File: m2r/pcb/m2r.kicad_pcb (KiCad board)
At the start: 2 copper layers, 87 parts, among them IC1 ADP3338, IC2 ADP3335, IC3 ADuM1201, IC4 ADuM1201, P1 CONN_2, P2 CONN_2, P7 CONN_2, X9 8M

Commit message: a good looking ratsnest
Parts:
- removed X9: 8M, Crystals:Crystal_HC49-U_Vertical
- added ANT1: JDGA_QUAD_V, m2r:JDGA_QUAD_V, F.Cu at (125.0, 61.5)
- added C35: 15p, m2r:C0603, F.Cu at (132.2, 110.2)
- added C36: 15p, m2r:C0603, F.Cu at (127.5, 110.2)
- added IC10: STM32F303C, m2r:LQFP48, F.Cu at (127.8, 102.0)
- added IC11: ADP3333, m2r:MSOP8, F.Cu at (119.8, 85.5)
- added IC5: ADuM1201, m2r:SOIC8, F.Cu at (137.2, 79.2)
- added IC6: MTX2, m2r:MTX2, F.Cu at (164.5, 98.0)
- added IC7: ADL5324, m2r:SOT89-3, F.Cu at (156.0, 81.5)
- added IC8: MAX-7Q, m2r:MAX-7Q, F.Cu at (127.0, 70.5)
- added IC9: ALM-2712, m2r:ALM-2712, F.Cu at (124.8, 67.8)
- added P3: CONN_4, m2r:S04B-PASK-2, F.Cu at (138.0, 125.5)
- added P4: CONN_4, m2r:S04B-PASK-2, F.Cu at (126.0, 125.5)
- added P5: CONN_4, m2r:S04B-PASK-2, F.Cu at (136.2, 67.0)
- added P6: SWD, m2r:FTSH-105-01-F-D-K, F.Cu at (121.0, 93.5)
- added P8: CONN_2, m2r:S02B-PASK-2, F.Cu at (146.0, 125.5)
- added TP21: TESTPAD, m2r:TESTPAD, F.Cu at (120.0, 68.2)
- added TP22: TESTPAD, m2r:TESTPAD, F.Cu at (141.0, 101.0)
- added TP23: TESTPAD, m2r:TESTPAD, F.Cu at (141.0, 103.0)
- added TP24: TESTPAD, m2r:TESTPAD, F.Cu at (141.0, 105.0)
- added TP25: TESTPAD, m2r:TESTPAD, F.Cu at (141.0, 107.0)
- added X10: 8M, m2r:HC49S, F.Cu at (132.2, 107.0)
- C1, C2, C24, C25, C27, C29, C3, C4, C7, C8: footprint Capacitors_SMD:c_0603 -> m2r:C0603
- C10: value 1n -> 2µ2; footprint Capacitors_SMD:c_0603 -> m2r:C0603
- C11, C30, C5, C6: value 2µ2 -> 100n; footprint Capacitors_SMD:c_0603 -> m2r:C0603
- C12: value 100n -> 1n; footprint Capacitors_SMD:c_0603 -> m2r:C0603
- C13, C32, C9: value 100n -> 2µ2; footprint Capacitors_SMD:c_0603 -> m2r:C0603
- C14: value 100p -> 100n; footprint Capacitors_SMD:c_0402 -> m2r:C0603
- C15: value 10n -> 100n; footprint Capacitors_SMD:c_0603 -> m2r:C0603
- C16: value 10µ -> 100p; footprint Capacitors_SMD:c_1206 -> m2r:C0402
- C17: value 10p -> 10n; footprint Capacitors_SMD:c_0402 -> m2r:C0603
- C18: value 20p -> 10µ; footprint Capacitors_SMD:c_0402 -> m2r:C1206
- C19: value 20p -> 10p; footprint Capacitors_SMD:c_0402 -> m2r:C0402
- C20: value 6.2p -> 20p; footprint Capacitors_SMD:c_0402 -> m2r:C0402
- C21: value 10µ -> 20p; footprint Capacitors_SMD:c_0603 -> m2r:C0402
- C22: value 100n -> 6.2p; footprint Capacitors_SMD:c_0603 -> m2r:C0402
- C23: value 100n -> 10µ; footprint Capacitors_SMD:c_0603 -> m2r:C0603
- C26: value 1µ -> 100n; footprint Capacitors_SMD:c_0603 -> m2r:C0603
- C28: value 100n -> 1µ; footprint Capacitors_SMD:c_0603 -> m2r:C0603
- C31: value 4µ7 -> 100n; footprint Capacitors_SMD:c_0603 -> m2r:C0603
- C33: value 15p -> 2µ2; footprint Capacitors_SMD:c_0603 -> m2r:C0603
- C34: value 15p -> 100n; footprint Capacitors_SMD:c_0603 -> m2r:C0603
- D1, D2, D3, D4, D5, D6: footprint Capacitors_SMD:c_0603 -> m2r:LED0603
- GS1, GS2: footprint Connect:GS3 -> m2r:SJ3
- IC1: footprint SMD_Packages:SOT223 -> m2r:SOT223
- IC2: footprint Housings_SSOP:MSOP-8 -> m2r:MSOP8
- IC3, IC4: footprint Housings_SOIC:SOIC-8_N -> m2r:SOIC8
- L1, L2: footprint SMD_Packages:SM0603 -> m2r:L0603
- L3: footprint SMD_Packages:SM0402 -> m2r:L0402
- P1, P2: footprint JST PA:S02B-PASK-2 -> m2r:S02B-PASK-2
- P7: value CONN_2 -> SMA; footprint JST PA:S02B-PASK-2 -> m2r:SMA-142-0701-801
- R1, R10, R11, R12, R13, R14, R2, R4, R5, R8, R9: footprint SMD_Packages:SM0603_Resistor -> m2r:R0603
- R3: footprint SMD_Packages:SM0402_r -> m2r:R0402
- R6: value 100 -> 6k8; footprint SMD_Packages:SM0603_Resistor -> m2r:R0603
- R7: value 6k8 -> 100; footprint SMD_Packages:SM0603_Resistor -> m2r:R0603
- TP1, TP10, TP11, TP12, TP13, TP14, TP15, TP16, TP17, TP18, TP19, TP2, TP20, TP3, TP4, TP5, TP6, TP7, TP8, TP9: footprint Measurement_Points:Measurement_Point_Round-SMD-Pad_Small -> m2r:TESTPAD
- moved C31 119.4 mm to (123.2, 68.2), turned to 180 degrees
- moved C32 115.9 mm to (118.5, 83.0)
- moved R6 113.6 mm to (123.2, 66.8), turned to 90 degrees
- moved C25 112.1 mm to (122.0, 101.5), turned to 180 degrees
- moved C33 109.3 mm to (126.5, 85.8), turned to 270 degrees
- moved C3 109.2 mm to (135.5, 75.8), turned to 90 degrees
- moved C30 107.8 mm to (123.2, 82.5), turned to 180 degrees
- moved C23 106.8 mm to (121.8, 104.8), turned to 180 degrees
- moved C11 106.7 mm to (135.5, 78.8), turned to 90 degrees
- moved C4 104.9 mm to (135.5, 73.0), turned to 90 degrees
- moved C26 104.4 mm to (130.8, 90.8), turned to 90 degrees
- moved C24 103.5 mm to (121.8, 103.0), turned to 180 degrees
- moved R14 103.3 mm to (127.5, 103.8)
- moved C5 99.3 mm to (126.8, 115.2), turned to 90 degrees
- moved C22 97.9 mm to (155.1, 69.2)
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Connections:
- C10 pad 1: +3.3V -> +5V
- C10 pad 2: Net-(C10-Pad2) -> GND
- C11 pad 1: BAT_MON -> +3.3V
- C12 pad 2: GND -> Net-(C12-Pad2)
- C13 pad 1: +3.3V -> BAT_MON
- C14 pad 1: +5V -> +3.3V
- C15 pad 1: +5V -> +3.3V
- C17 pad 1: Net-(C17-Pad1) -> +5V
- C17 pad 2: Net-(C17-Pad2) -> GND
- C18 pad 1: Net-(C18-Pad1) -> +5V
- C18 pad 2: Net-(C18-Pad2) -> GND
- C19 pad 1: GND -> Net-(C19-Pad1)
- C19 pad 2: Net-(C17-Pad1) -> Net-(C19-Pad2)
- C2 pad 1: GND -> Net-(C2-Pad1)
- C2 pad 2: +3.3V -> Net-(C2-Pad2)
- C20 pad 1: GND -> Net-(C20-Pad1)
- C20 pad 2: Net-(C18-Pad1) -> Net-(C20-Pad2)
- C21 pad 1: +3.3V -> GND
- C21 pad 2: GND -> Net-(C19-Pad1)
- C22 pad 1: +3.3V -> GND
- C22 pad 2: GND -> Net-(C20-Pad1)
- C29 pad 1: Net-(C29-Pad1) -> +3.3V
- C3 pad 2: +5V -> +3.3V
- C31 pad 1: Net-(C29-Pad1) -> Net-(C31-Pad1)
- C32 pad 1: nRST -> Net-(C31-Pad1)
- C33 pad 1: Net-(C33-Pad1) -> +3.3V
- C34 pad 1: Net-(C34-Pad1) -> nRST
- C4 pad 1: +3.3V -> GND
- C4 pad 2: GND -> +5V
- C5 pad 1: +BATT -> GND
- C5 pad 2: GND -> +3.3V
- C8 pad 1: +5V -> +3.3V
- C9 pad 1: +3.3V -> +BATT
- GS1 pad 3: Net-(C17-Pad2) -> Net-(C19-Pad2)
- GS2 pad 1: Net-(C18-Pad2) -> Net-(C20-Pad2)
- IC2 pad 5: Net-(C10-Pad2) -> Net-(C12-Pad2)
- IC3 pad 5: Net-(C1-Pad1) -> Net-(C2-Pad1)
- IC3 pad 8: Net-(C1-Pad2) -> Net-(C2-Pad2)
- IC4 pad 2: RB_TX -> GPS_RX
- IC4 pad 3: RB_RX -> GPS_TX
- IC4 pad 5: GND -> Net-(C1-Pad1)
- IC4 pad 8: +3.3V -> Net-(C1-Pad2)
- L2 pad 2: Net-(C17-Pad1) -> Net-(C19-Pad1)
- L3 pad 1: Net-(C18-Pad1) -> Net-(C20-Pad1)
- P1 pad 1: GND -> Net-(P1-Pad1)
- P1 pad 2: Net-(P1-Pad2) -> GND
- P2 pad 1: Net-(P1-Pad2) -> +BATT
- P2 pad 2: +BATT -> Net-(P1-Pad1)
- P7 pad 1: Net-(P7-Pad1) -> Net-(GS2-Pad2)
- P7 pad 2: LED_C -> GND
- R14 pad 1: Net-(C34-Pad1) -> Net-(C36-Pad1)
- R4 pad 1: Net-(P7-Pad1) -> Net-(P8-Pad1)
- R5 pad 1: Net-(P7-Pad1) -> Net-(P8-Pad1)
- R6 pad 1: Net-(D2-Pad1) -> Net-(C31-Pad1)
- R6 pad 2: Net-(R6-Pad2) -> Net-(IC9-Pad11)
- R7 pad 1: Net-(C29-Pad1) -> Net-(D2-Pad1)
- R7 pad 2: Net-(IC8-Pad11) -> Net-(R7-Pad2)
- R9 pad 1: Net-(R6-Pad2) -> Net-(R7-Pad2)
- TP10 pad 1: RB_RX -> Net-(IC5-Pad6)
- TP11 pad 1: RB_TX -> +BATT
- TP12 pad 1: NTX2B_TXD -> GND
- TP13 pad 1: NTX2B_P1 -> BAT_MON
- TP14 pad 1: NTX2B_P0 -> RB_RX
- TP15 pad 1: NTX2B_EN -> RB_TX
- TP18 pad 1: Net-(C29-Pad1) -> Net-(C31-Pad1)
- TP19 pad 1: GPS_RX -> GPS_RESET
- TP20 pad 1: GPS_TX -> GPS_SCL
- TP4 pad 1: Net-(IC3-Pad6) -> GPS_RX
- TP6 pad 1: Net-(IC4-Pad6) -> Net-(IC3-Pad6)
- TP7 pad 1: +BATT -> GPS_TX
- TP8 pad 1: GND -> Net-(IC4-Pad6)
- TP9 pad 1: BAT_MON -> Net-(IC5-Pad7)
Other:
- board outline added: 50 x 75 mm

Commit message: further pcb work i guess
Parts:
- added D10: ESD5V3S1U, m2r:TSLP-2-17, F.Cu at (142.0, 121.0)
- added D11: ESD5V3S1U, m2r:TSLP-2-17, F.Cu at (146.0, 121.0)
- added D7: ESD5V3S1U, m2r:TSLP-2-17, F.Cu at (141.0, 71.5)
- added D8: ESD5V3S1U, m2r:TSLP-2-17, F.Cu at (150.8, 121.0)
- added D9: ESD5V3S1U, m2r:TSLP-2-17, F.Cu at (156.5, 65.3)
- added X11: M3 MOUNT, m2r:M3_MOUNT, F.Cu at (121.0, 117.0)
- added X12: M3 MOUNT, m2r:M3_MOUNT, F.Cu at (161.0, 74.0)
- added X13: M3 MOUNT, m2r:M3_MOUNT, F.Cu at (121.0, 74.0)
- added X14: M3 MOUNT, m2r:M3_MOUNT, F.Cu at (161.0, 117.0)
- moved TP2 35.8 mm to (144.2, 83.1)
- moved C10 34.7 mm to (142.5, 94.0), turned to 180 degrees
- moved IC1 33.0 mm to (143.2, 91.8), turned to 0 degrees
- moved C8 28.5 mm to (152.5, 111.2), turned to 180 degrees
- moved R9 27.9 mm to (137.5, 89.8), turned to 270 degrees
- moved R7 27.2 mm to (136.2, 89.8), turned to 270 degrees
- moved C9 24.3 mm to (145.2, 94.0)
- moved C30 18.2 mm to (135.5, 69.1)
- moved D6 14.3 mm to (130.0, 88.5), turned to 90 degrees
- moved D5 13.2 mm to (131.2, 88.5), turned to 90 degrees
- moved R13 12.9 mm to (130.0, 89.8), turned to 270 degrees
- moved TP20 12.4 mm to (125.5, 78.5)
- moved D4 12.2 mm to (132.5, 88.5), turned to 90 degrees
- moved R12 11.6 mm to (131.2, 89.8), turned to 270 degrees
- moved D3 11.5 mm to (133.8, 88.5), turned to 90 degrees
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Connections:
- IC10 pad 14: LED_A -> LED_C
- IC10 pad 15: LED_C -> LED_A
- P1 pad 1: Net-(P1-Pad1) -> GND
- P1 pad 2: GND -> Net-(P1-Pad2)
- P2 pad 1: +BATT -> Net-(P1-Pad2)
- P2 pad 2: Net-(P1-Pad1) -> +BATT
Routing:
- net GND: track 0.00 -> 84.9 mm, vias 0 -> 40
- net +BATT: track 0.00 -> 49.4 mm
- net +3.3V: track 0.00 -> 12.5 mm
- net +5V: track 0.00 -> 8.64 mm
- net Net-(P1-Pad2): track 0.00 -> 6.00 mm
- net Net-(D9-Pad1): track 0.00 -> 5.64 mm
- net BAT_MON: track 0.00 -> 4.43 mm
- net Net-(C12-Pad2): track 0.00 -> 1.65 mm
- added copper zone on B.Cu, net GND
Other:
- net class Default: clearance 0.254 -> 0.2; trace_width 0.254 -> 0.2; via_dia 0.889 -> 0.8; via_drill 0.635 -> 0.6
- rule trace_clearance: 0.254 -> 0.2
- rule trace_min: 0.254 -> 0.2
- rule via_min_drill: 0.508 -> 0.6
- rule via_min_size: 0.889 -> 0.8

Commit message: 2 airwires to go
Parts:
- moved D10 20.0 mm to (162.0, 121.4), turned to 180 degrees
- moved P8 16.0 mm to (162.0, 125.8)
- moved R4 14.0 mm to (157.2, 121.5)
- moved D11 14.0 mm to (160.0, 121.4), turned to 0 degrees
- moved C35 13.4 mm to (119.9, 105.0), turned to 270 degrees
- moved TP19 12.5 mm to (136.8, 69.0)
- moved C8 12.3 mm to (140.2, 112.2)
- moved IC2 12.3 mm to (141.8, 114.0)
- moved C7 12.3 mm to (140.2, 120.0)
- moved C30 12.2 mm to (133.5, 81.1), turned to 0 degrees
- moved R1 11.7 mm to (137.8, 107.8), turned to 270 degrees
- moved R5 11.3 mm to (156.0, 121.5)
- moved TP13 9.96 mm to (137.8, 106.5)
- moved C34 9.95 mm to (121.0, 100.8), turned to 180 degrees
- moved R2 9.92 mm to (139.0, 107.8), turned to 270 degrees
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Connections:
- IC10 pad 14: LED_C -> LED_A
- IC10 pad 15: LED_A -> LED_C
- P8 pad 1: Net-(D11-Pad1) -> LED_C
- P8 pad 2: LED_C -> Net-(D11-Pad1)
- R9 pad 1: Net-(R7-Pad2) -> +5V
- R9 pad 2: +5V -> Net-(R7-Pad2)
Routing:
- net +3.3V: track 12.5 -> 188.9 mm
- net GND: track 84.9 -> 184.1 mm, vias 40 -> 36
- net +5V: track 8.64 -> 65.6 mm, vias 0 -> 2
- net LED_C: track 0.00 -> 46.5 mm, vias 0 -> 2
- net GPS_RESET: track 0.00 -> 40.1 mm, vias 0 -> 2
- net LED_A: track 0.00 -> 36.8 mm, vias 0 -> 2
- net nRST: track 0.00 -> 35.6 mm
- net Net-(GS1-Pad1): track 0.00 -> 31.3 mm
- net GPS_SDA: track 0.00 -> 29.1 mm, vias 0 -> 2
- net RB_TX: track 0.00 -> 27.4 mm, vias 0 -> 2
- net RB_RX: track 0.00 -> 26.7 mm, vias 0 -> 2
- net GPS_SCL: track 0.00 -> 25.8 mm, vias 0 -> 2
- net Net-(C31-Pad1): track 0.00 -> 21.9 mm
- net Net-(C1-Pad1): track 0.00 -> 16.3 mm
- net NTX2B_TXD: track 0.00 -> 15.5 mm, vias 0 -> 1
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
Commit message: 0 airwires!
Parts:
- moved D1 1.07 mm to (135.5, 87.5)
- moved D2 1.07 mm to (136.8, 87.5)
- moved D3 1.07 mm to (134.2, 87.5)
- moved D4 1.07 mm to (131.8, 87.5)
- moved D5 1.07 mm to (133.0, 87.5)
- moved D6 1.07 mm to (130.5, 87.5)
- moved R10 1.07 mm to (134.2, 88.8)
- moved R11 1.07 mm to (131.8, 88.8)
- moved R12 1.07 mm to (133.0, 88.8)
- moved R13 1.07 mm to (130.5, 88.8)
- moved R7 1.07 mm to (136.8, 88.8)
- moved R8 1.07 mm to (135.5, 88.8)
- moved R9 1.07 mm to (138.0, 88.8)
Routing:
- net GPS_RX: track 2.01 -> 69.2 mm, vias 0 -> 4
- net GPS_TX: track 2.02 -> 64.3 mm, vias 0 -> 4
- net nRST: track 35.6 -> 14.0 mm, vias 0 -> 2
- net +3.3V: track 188.9 -> 199.8 mm
- net RB_RX: track 26.7 -> 28.4 mm
- net +5V: track 65.6 -> 67.2 mm
- net GND: track 184.1 -> 182.9 mm, vias 36 -> 37
- net LED_1: track 2.36 -> 3.50 mm
- net LED_2: track 2.25 -> 3.32 mm
- net LED_3: track 2.54 -> 3.29 mm
- net GPS_SDA: track 29.1 -> 28.4 mm
- net SWO: track 5.61 -> 6.11 mm
- net SWDIO: track 9.16 -> 9.57 mm, vias 0 -> 2

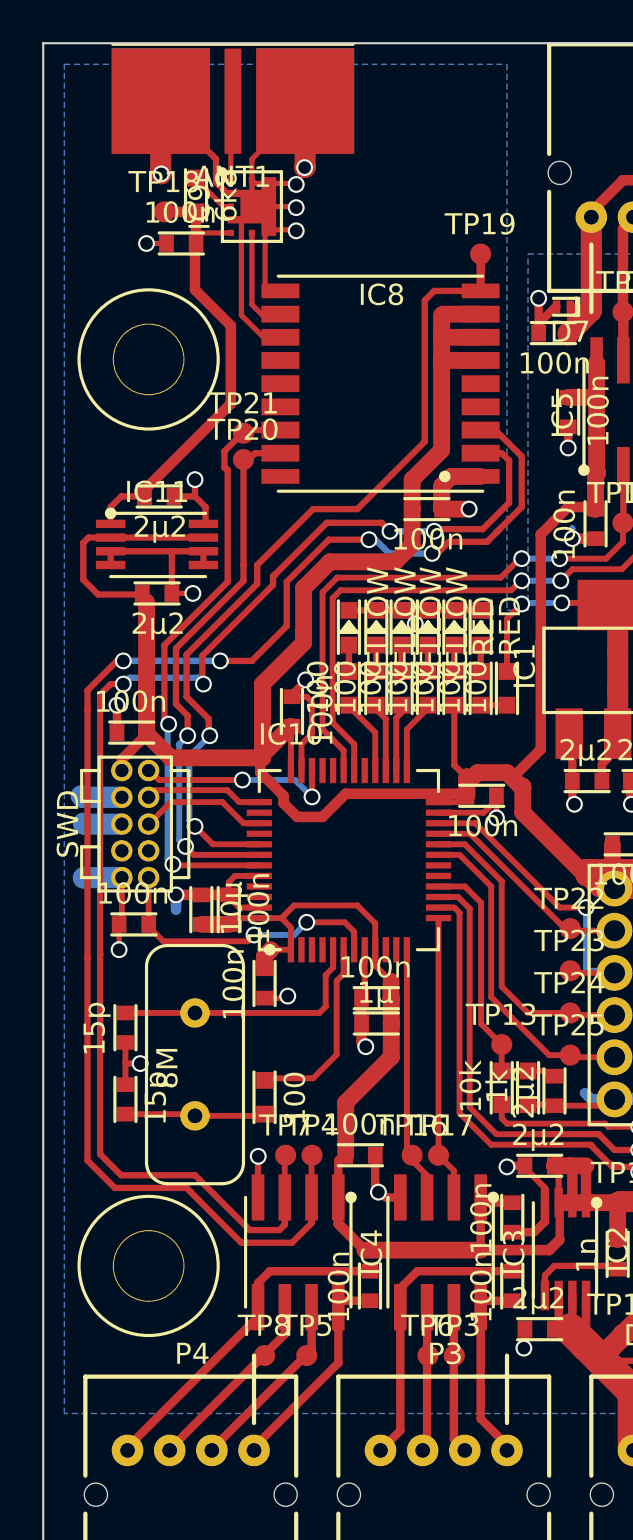
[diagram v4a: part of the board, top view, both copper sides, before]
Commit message: gps top gnd plane
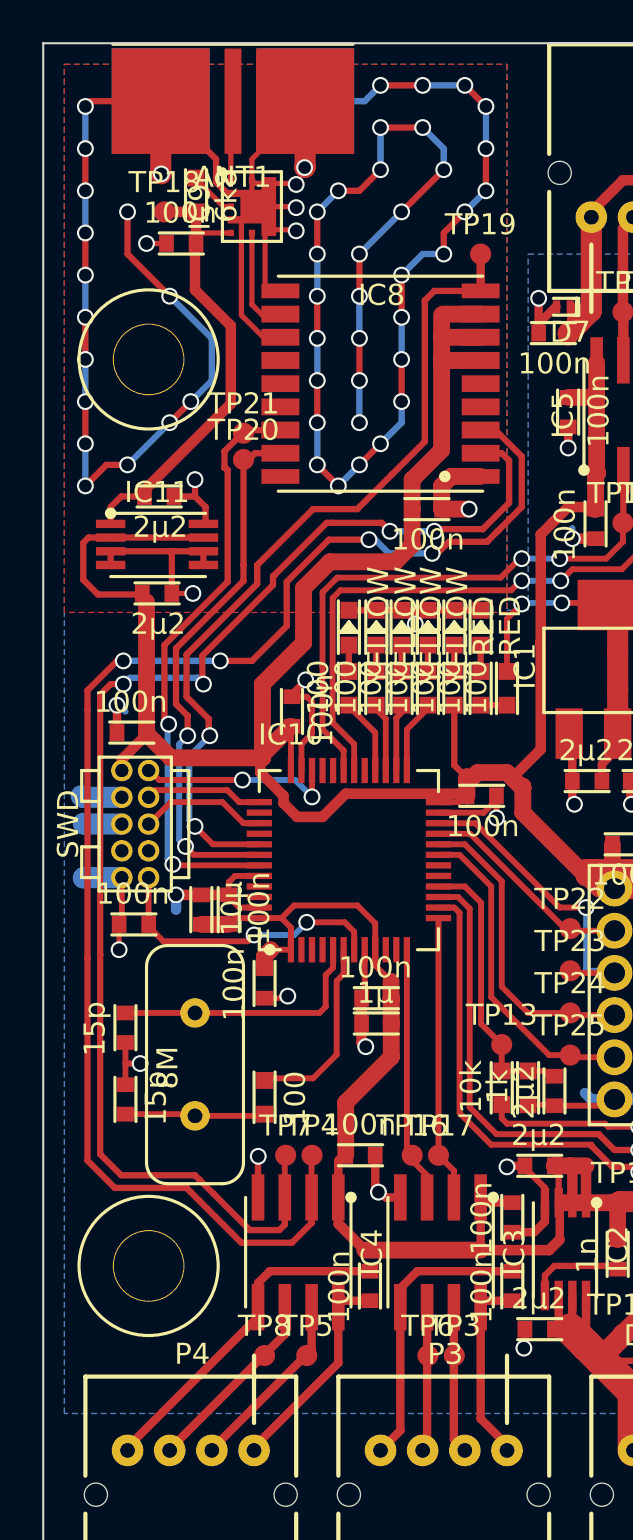
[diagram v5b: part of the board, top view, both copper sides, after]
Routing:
- net GND: track 182.9 -> 290.9 mm, vias 37 -> 85
- added copper zone on F.Cu, net GND

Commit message: pretty silk
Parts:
- added G***: LOGO, m2r:cusf_logo, F.Cu at (162.4, 87.5)
- added G***: LOGO, m2r:cusf_logo_full, B.Cu at (139.5, 95.9)
- C22: value 6.2p -> 6p2
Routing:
- net GPS_RX: track 69.2 -> 68.3 mm
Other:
- board text added: "3V"
- board text added: "5V"
- board text added: "ARM"
- board text added: "BAT"
- board text added: "FC"
- board text added: "GPS"
- board text added: "LED"
- board text added: "MARTLET 2 RADIO"
- board text added: "R1 ADAM GREIG 2014-07-23"
- board text added: "RADIO"
- board text added: "RB"
- board text added: "STATUS"
- board text added: "cusf.co.uk"
